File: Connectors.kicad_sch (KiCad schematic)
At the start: 2 parts, among them J1 MR60PW, J2 MR60PW

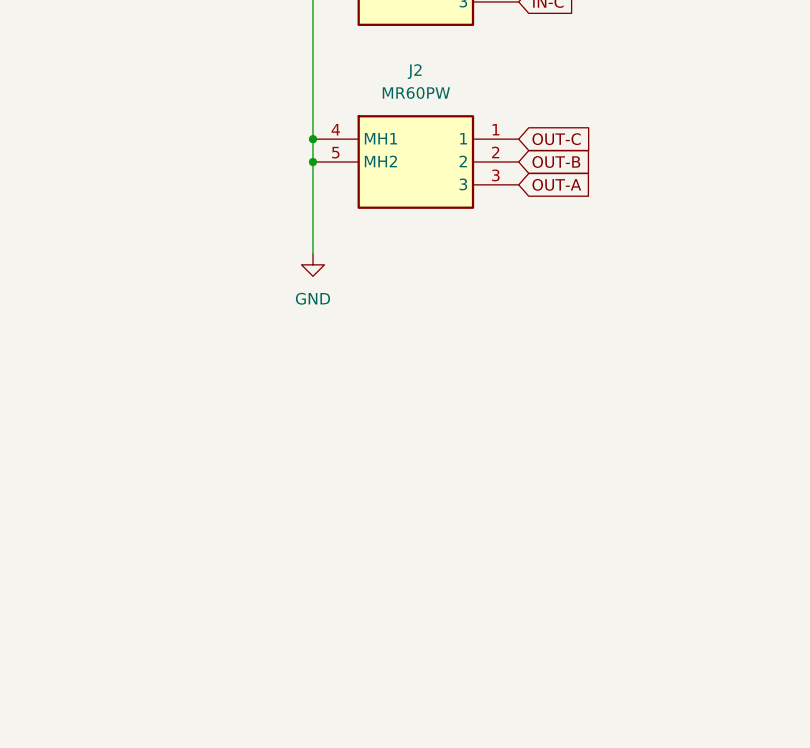
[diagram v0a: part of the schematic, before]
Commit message: Fix the +2.5VA reference, add XT60PW-M connectors, predict measurement quality
- IC3: LTC6655LN-2.5 replaced by the standard LTC6655-2.5, pin 6 is now
  VOUT_S tied to VOUT_F (the LN version has NR on that pin)
- R12: 49.9k -> 24.9k on the SET pin of IC9, +2.5VA = 2.500 V instead of
  2.549 V; both points removed from the README design review
- J5, J6: two Amass XT60PW-M added on the Connectors sheet and on the PCB,
  with symbol, footprint and 3D model in lib/. Their power pins are not
  wired yet
- Simulations 07 (ESC PWM waveforms through both channels) and 08 (Monte
  Carlo on the tolerances), analysed by measurement_quality.py into
  measurement_quality.md; plot style shared in plotstyle.py
- Simulations 01, 02, 04, results.md and their figures redone for the
  corrected rail
- README, README template and CHANGELOG updated; all sheets re-saved from
  KiCad

Co-Authored-By: Claude Opus 5.5 <noreply@anthropic.com>
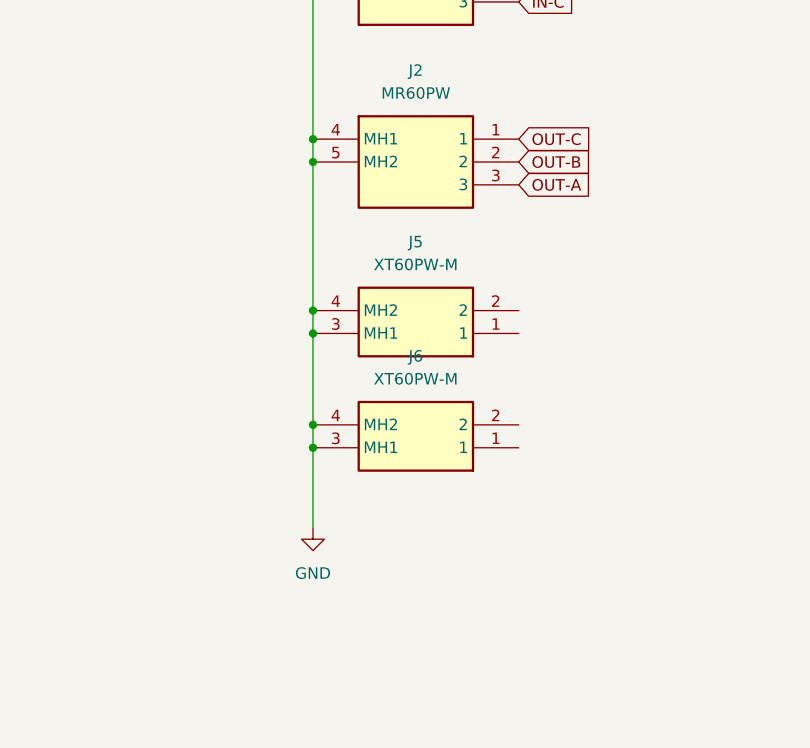
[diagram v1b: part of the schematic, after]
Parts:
- added J5, J6: XT60PW-M, PhaseSense-8586:XT60PWM, symbol PhaseSense-8586:XT60PW-M
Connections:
- net GND: now also J5.3 (MH1), J5.4 (MH2), J6.3 (MH1), J6.4 (MH2)

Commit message: Rename the project to OPEN_PHASE
PhaseSense-8586 was named after the first parts of the design (INA240 +
ADS8586S), which are no longer on the board. OPEN_PHASE follows
OPEN_WEIGHT, the other OPEN THRUST LAB board.

- project files: OPEN_PHASE.kicad_pro / _sch / _pcb / _prl / _dru
- libraries: lib/lib_sym/OPEN_PHASE.kicad_sym and
  lib/lib_fp/OPEN_PHASE.pretty, nickname OPEN_PHASE in both tables, in
  every lib_id and in every footprint of the PCB
- project name of every symbol and sheet instance, so the reference
  designators are kept
- PROJECT_NAME and GIT_URL in the project and in kibot_main.yaml, README
  and its template, CHANGELOG, LTspice headers and their generator
- the README note now says the project was first published as
  PhaseSense-8586

The GitHub repository is now foukouda/OPEN_PHASE. The board name
PHASETRACKER is unchanged. The netlist, ERC and DRC reports are the same
before and after the rename.

Co-Authored-By: Claude Opus 5.5 <noreply@anthropic.com>
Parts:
- J1, J2: footprint PhaseSense-8586:MR60PW -> OPEN_PHASE:MR60PW; symbol PhaseSense-8586:MR60PW -> OPEN_PHASE:MR60PW
- J5, J6: footprint PhaseSense-8586:XT60PWM -> OPEN_PHASE:XT60PWM; symbol PhaseSense-8586:XT60PW-M -> OPEN_PHASE:XT60PW-M
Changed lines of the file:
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@@
 	)
 	(symbol
-		(lib_id "PhaseSense-8586:XT60PW-M")
+		(lib_id "OPEN_PHASE:XT60PW-M")
 		(at 209.55 104.14 180)
 		(unit 1)
@@
 			)
 		)
-		(property "Footprint" "PhaseSense-8586:XT60PWM"
+		(property "Footprint" "OPEN_PHASE:XT60PWM"
 			(at 190.5 9.22 0)
 			(hide yes)
@@
 		)
 		(instances
-			(project "PhaseSense-8586"
+			(project "OPEN_PHASE"
 				(path "/f9e05184-c88b-4a88-ae9c-ab2bdb32be7c/c5103ceb-5325-4a84-a025-9638a412984e/c7c721f5-c1ee-4db1-9a46-4881d72bcc61"
 					(reference "J6")
@@
 	)
 	(symbol
-		(lib_id "PhaseSense-8586:MR60PW")
+		(lib_id "OPEN_PHASE:MR60PW")
 		(at 186.69 49.53 0)
 		(unit 1)
@@
 			)
 		)
-		(property "Footprint" "PhaseSense-8586:MR60PW"
+		(property "Footprint" "OPEN_PHASE:MR60PW"
 			(at 205.74 144.45 0)
 			(hide yes)
@@
 		)
 		(instances
-			(project "PhaseSense-8586"
+			(project "OPEN_PHASE"
 				(path "/f9e05184-c88b-4a88-ae9c-ab2bdb32be7c/c5103ceb-5325-4a84-a025-9638a412984e/c7c721f5-c1ee-4db1-9a46-4881d72bcc61"
 					(reference "J1")
@@
 		)
 		(instances
-			(project "PhaseSense-8586"
+			(project "OPEN_PHASE"
 				(path "/f9e05184-c88b-4a88-ae9c-ab2bdb32be7c/c5103ceb-5325-4a84-a025-9638a412984e/c7c721f5-c1ee-4db1-9a46-4881d72bcc61"
 					(reference "#PWR03")
@@
 	)
 	(symbol
-		(lib_id "PhaseSense-8586:XT60PW-M")
+		(lib_id "OPEN_PHASE:XT60PW-M")
 		(at 209.55 91.44 180)
 		(unit 1)
@@
 			)
 		)
-		(property "Footprint" "PhaseSense-8586:XT60PWM"
+		(property "Footprint" "OPEN_PHASE:XT60PWM"
 			(at 190.5 -3.48 0)
 			(hide yes)
@@
 		)
 		(instances
-			(project "PhaseSense-8586"
+			(project "OPEN_PHASE"
 				(path "/f9e05184-c88b-4a88-ae9c-ab2bdb32be7c/c5103ceb-5325-4a84-a025-9638a412984e/c7c721f5-c1ee-4db1-9a46-4881d72bcc61"
 					(reference "J5")
@@
 	)
 	(symbol
-		(lib_id "PhaseSense-8586:MR60PW")
+		(lib_id "OPEN_PHASE:MR60PW")
 		(at 186.69 69.85 0)
 		(unit 1)
@@
 			)
 		)
-		(property "Footprint" "PhaseSense-8586:MR60PW"
+		(property "Footprint" "OPEN_PHASE:MR60PW"
 			(at 205.74 164.77 0)
 			(hide yes)
@@
 		)
 		(instances
-			(project "PhaseSense-8586"
+			(project "OPEN_PHASE"
 				(path "/f9e05184-c88b-4a88-ae9c-ab2bdb32be7c/c5103ceb-5325-4a84-a025-9638a412984e/c7c721f5-c1ee-4db1-9a46-4881d72bcc61"
 					(reference "J2")

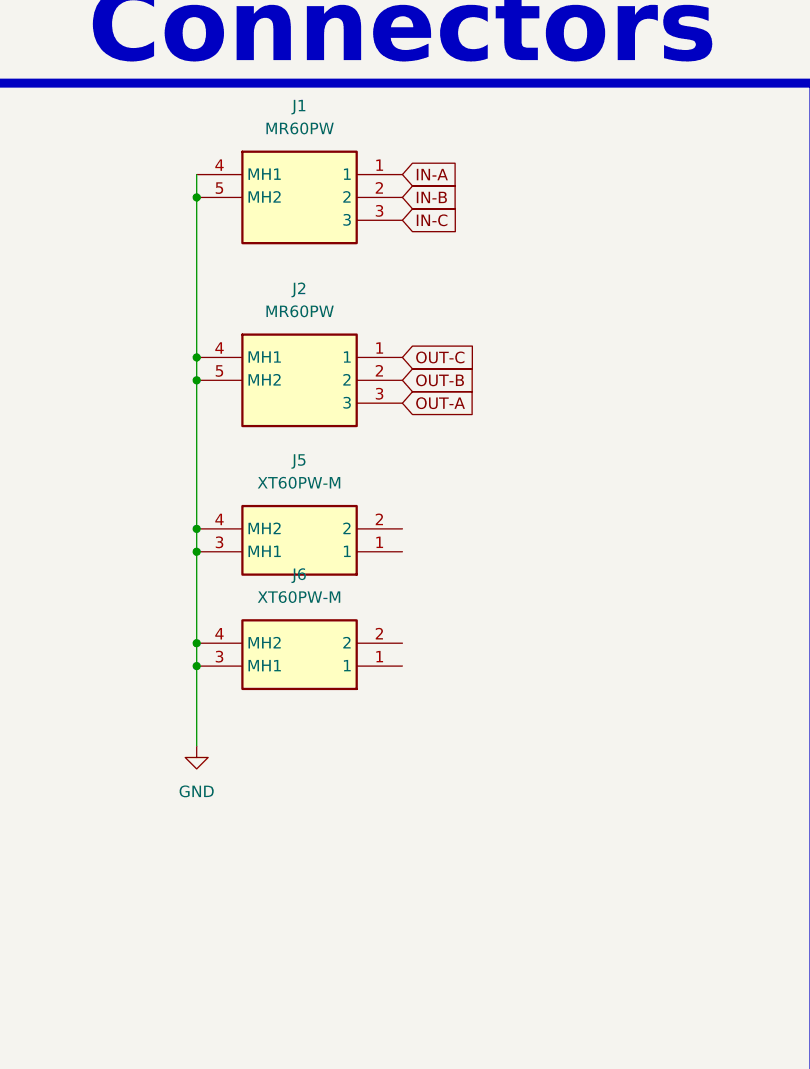
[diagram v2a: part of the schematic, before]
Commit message: Smaller boost inductor, white board, openEMS and thermal simulations
- L1: Wurth 744373965022 (13.5 x 12.5 mm) -> WE-MAPI 4030 74438357022
  (2.2 uH, 4.1 x 4.1 x 3.1 mm, Isat 4.6 A at -10 %, above the 3.1 A LT8362
  switch limit). Footprint and STEP from the KiCad library, copied to lib/.
- Board: solder mask white (custom opaque #F4F4F0F5, the KiCad "White"
  preset renders pink over copper), silkscreen black. kibot_globals.yaml
  names the colours so the fabrication notes print WHITE / BLACK.
- Simulation/openEMS: inductance of the PBV shunts seen by the INA241
  inputs on the routed copper (results.md, figures in Images/Simulation).
- Simulation/Thermal: current density and temperature of the power paths.
- LTspice simulations, figures and README updated; sim07 DC bus figure.
- 3D animation (Images/OPEN_PHASE.mp4, OPEN_PHASE-spin.gif) on the white board.
- XT60PW-F footprint and model, bottom silkscreen cartouches.

Co-Authored-By: Claude Opus 5.5 <noreply@anthropic.com>
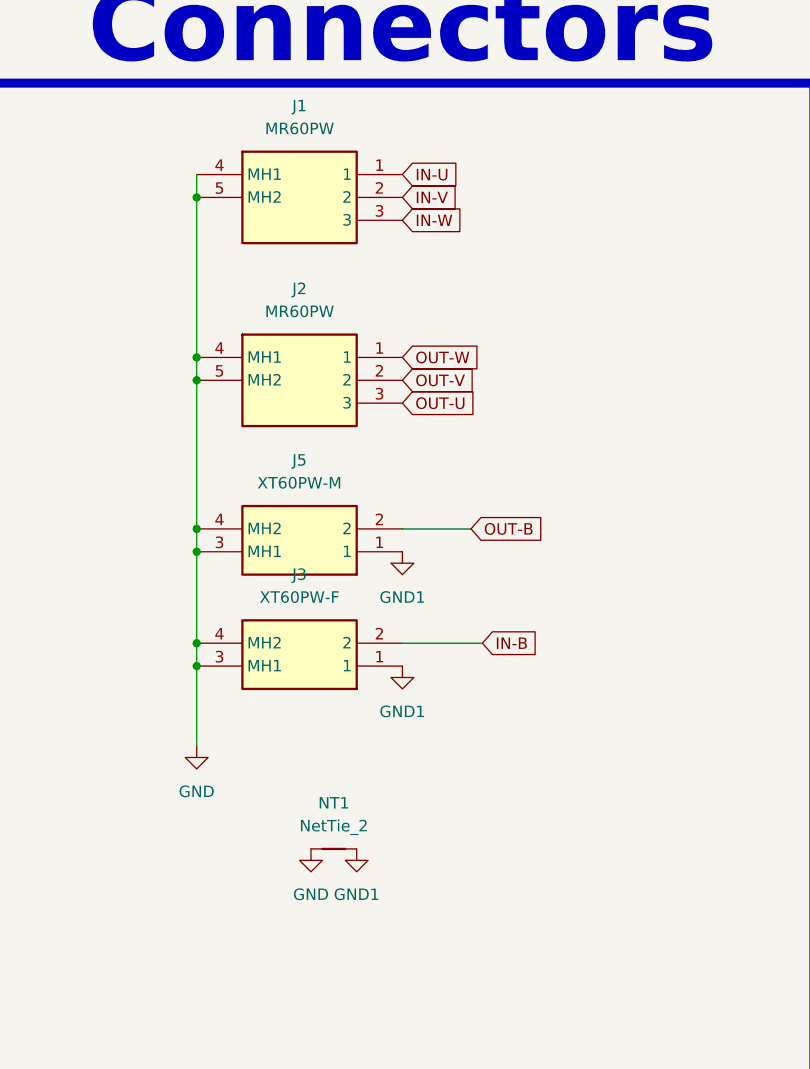
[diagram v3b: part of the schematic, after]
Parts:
- removed J6: XT60PW-M, OPEN_PHASE:XT60PWM, symbol OPEN_PHASE:XT60PW-M
- added J3: XT60PW-F, OPEN_PHASE:AMASS_XT60PW-F_1x02_P7.20mm_Horizontal, symbol OPEN_PHASE:XT60PW-F
- added NT1: NetTie_2, NetTie:NetTie-2_SMD_Pad0.5mm, symbol Device:NetTie_2
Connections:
- net GND: now also J3.3 (MH1), J3.4 (MH2), NT1.1
- net IN-B: now also J3.2; no longer J1.2
- net OUT-B: now also J5.2; no longer J2.2
- net GND1: now reaches J5.1
- net GND1: now also J3.1, NT1.2
- net IN-A renamed IN-U
- net IN-C renamed IN-W
- net OUT-A renamed OUT-U
- net OUT-C renamed OUT-W
- new net IN-V: J1.2
- new net OUT-V: J2.2

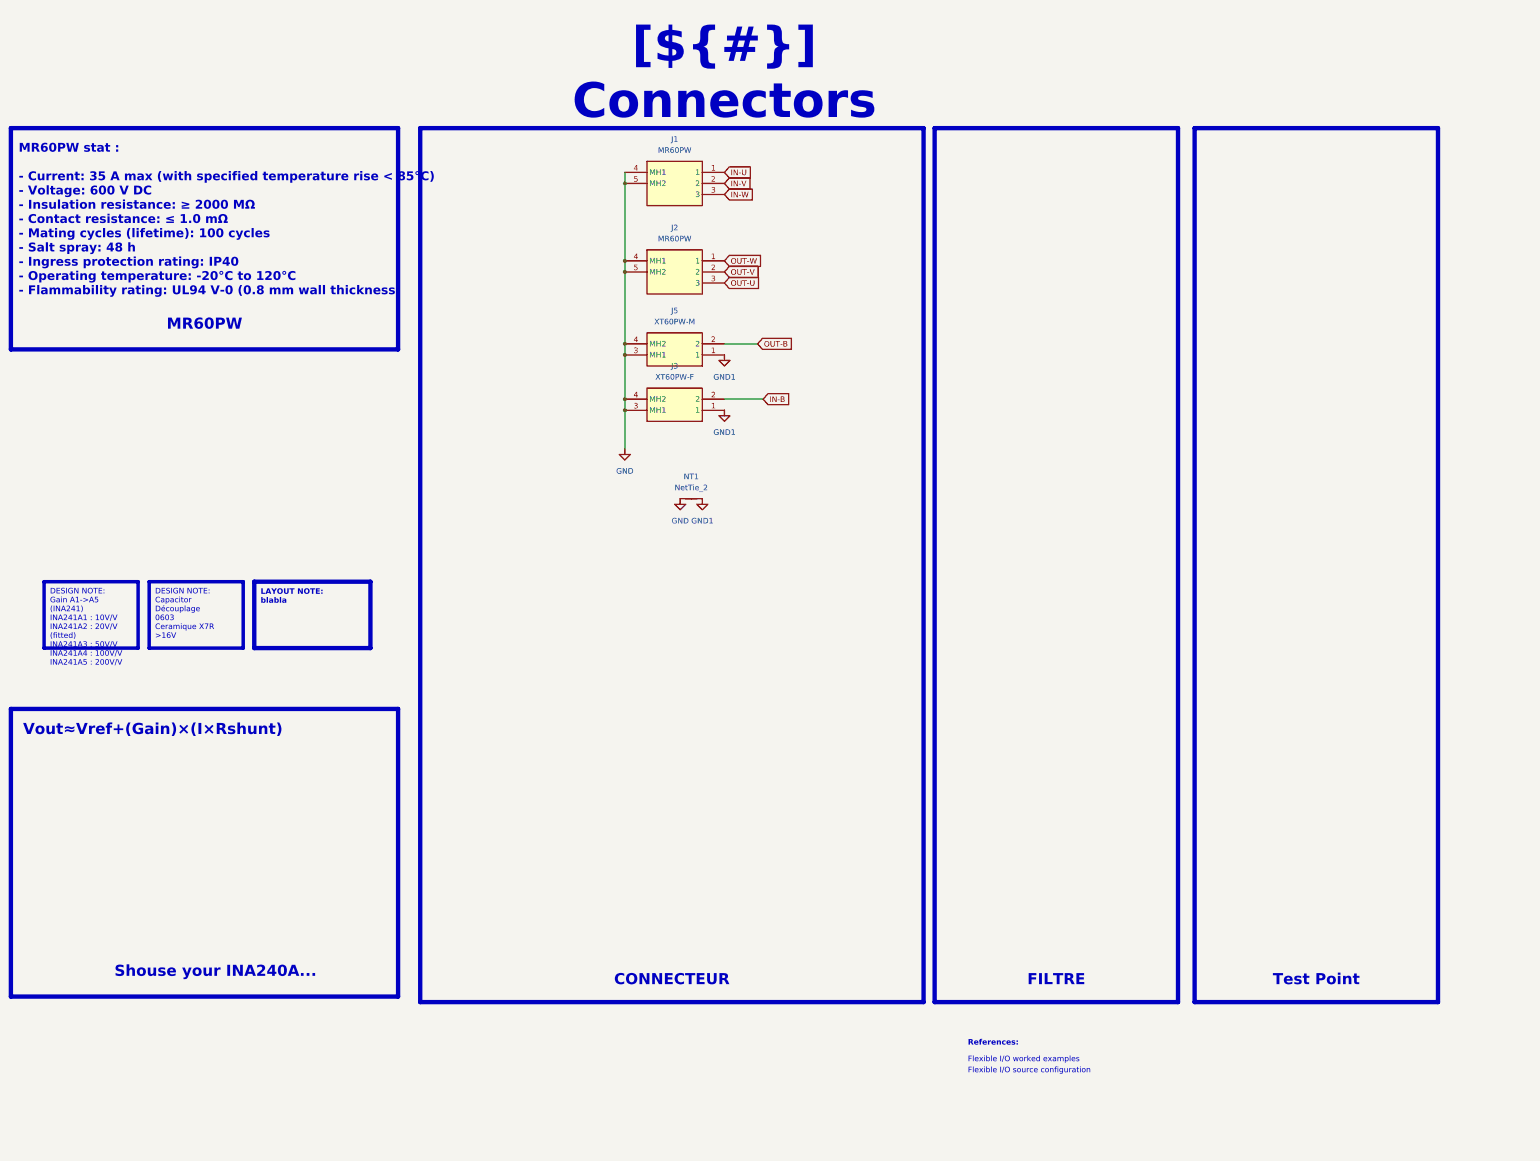
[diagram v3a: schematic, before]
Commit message: Restyle schematic sheets, new title block logo, WE-MAPI inductor in simulations
- Schematic sheets: restyled frames, tables and text boxes
- Title block: INGENIERIE FRANCE logo in KDT_Template_GIT.kicad_wks
- LTspice: L1 modelled as WE-MAPI 4030 74438357022 (22 mOhm),
  simulations 01 and 03 rerun, README and results updated

Co-Authored-By: Claude Opus 5.5 <noreply@anthropic.com>
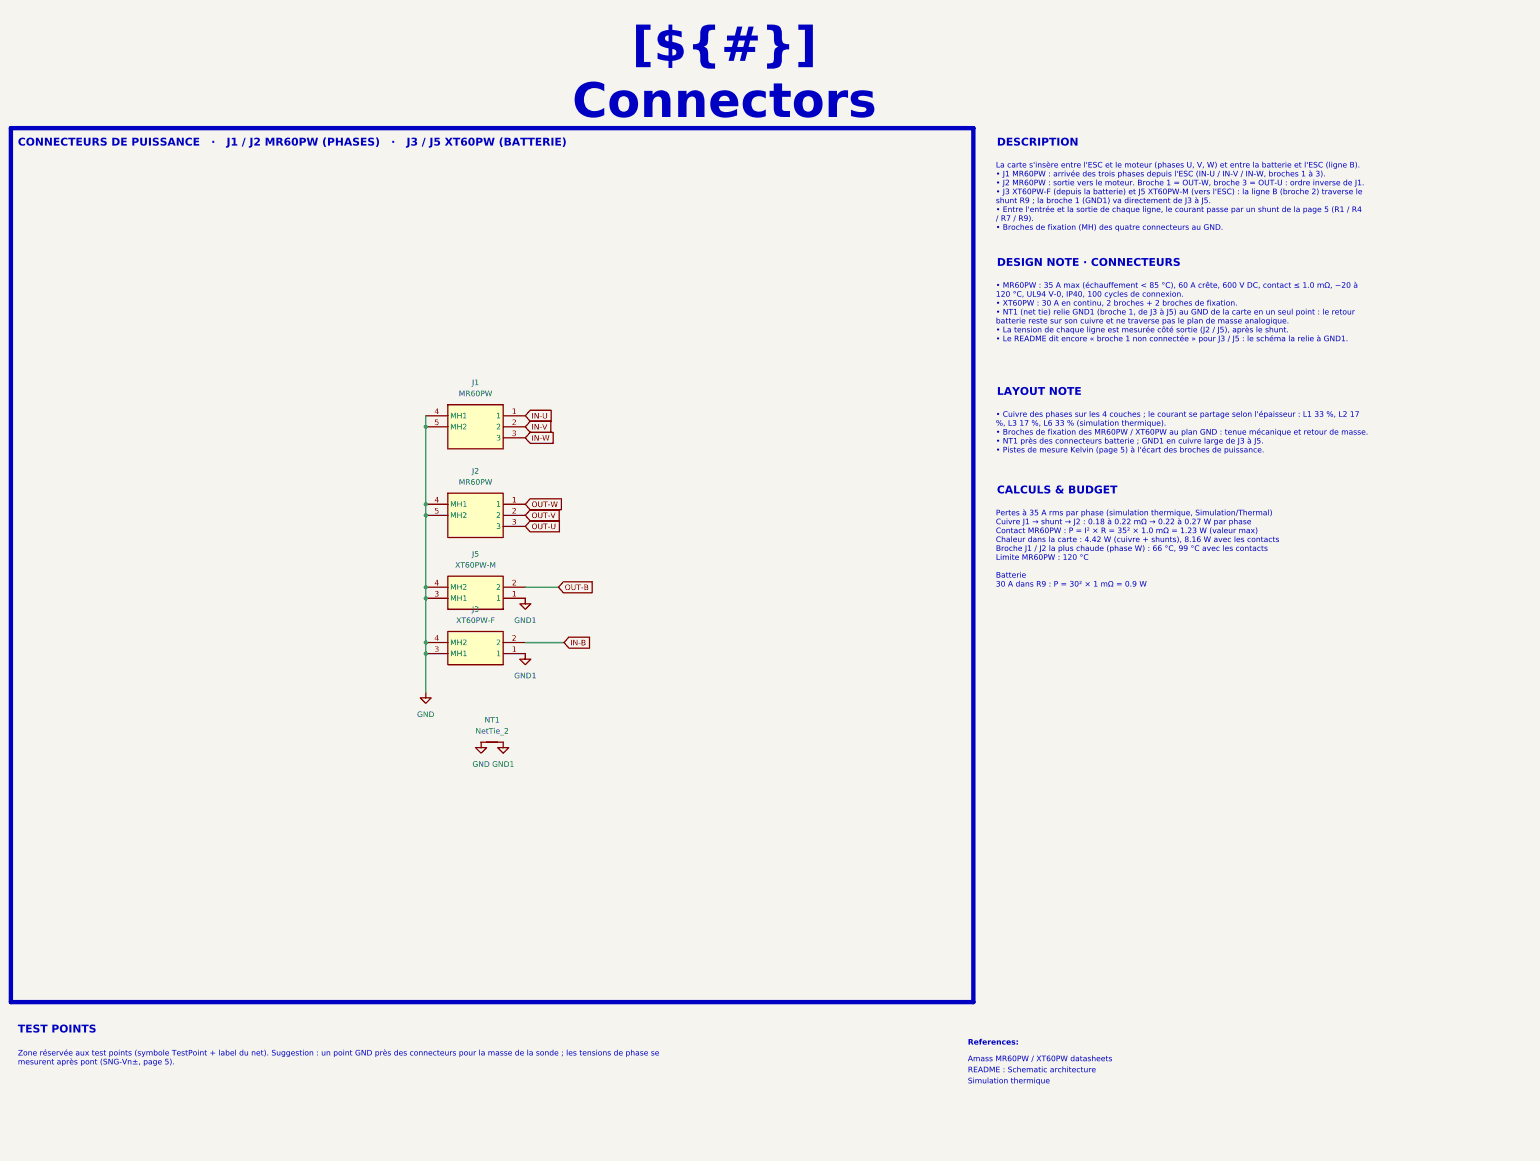
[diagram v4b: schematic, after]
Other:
- note added: "Amass MR60PW / XT60PW datasheets"
- note added: "README : Schematic architecture"
- note added: "Simulation thermique"
- note removed: "Flexible I/O source configuration"
- note removed: "Flexible I/O worked examples"
- note removed: "MR60PW stat : - Current: 35 A max (with specified temperature rise < 85°C) - Voltage: 600 V DC - Insulation resistance: ≥ 2000 MΩ - Contact resistance: ≤ 1.0 mΩ - Mating cycles (lifetime): 100 cycles - Salt spray: 48 h - Ingress protection rating: IP40 - Operating temperature: -20°C to 120°C - Flammability rating: UL94 V-0 (0.8 mm wall thickness)"
- note removed: "Vout≈Vref+(Gain)×(I×Rshunt)"
- moved on the sheet: J1, J2, J3, J5, NT1
